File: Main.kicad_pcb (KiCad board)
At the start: 2 copper layers, 39 parts, among them J1 Conn_01x01_Female, J2 Conn_01x01_Female, J3 Conn_01x01_Female, J4 Conn_01x02_Female, J5 Conn_01x01_Female, Q1 CSD17307Q5A, Q2 CSD17307Q5A, Q3 Si6435ADQ, SW1 SW_Push, SW2 SW_Push, SW3 SW_Push, U1 LTC4002ES8-4.2, U2 BQ297xy, U3 LTC6995-1, U4 TPS2557

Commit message: finished traces
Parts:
- SW3: footprint Button_Switch_SMD:SW_SPST_B3U-1000P -> Button_Switch_SMD:SW_DIP_SPSTx01_Slide_6.7x4.1mm_W6.73mm_P2.54mm_LowProfile_JPin
- moved D2 188.3 mm to (217.4, 100.2), turned to 270 degrees
- moved TP1 180.4 mm to (217.4, 114.9)
- moved C3 177.9 mm to (210.0, 125.9)
- moved TP3 177.3 mm to (226.4, 103.6)
- moved D1 177.2 mm to (204.3, 98.7), turned to 180 degrees
- moved TP2 176.5 mm to (217.2, 125.9)
- moved C5 174.3 mm to (195.3, 73.3)
- moved J4 174.0 mm to (210.6, 73.0)
- moved R1 173.0 mm to (198.5, 98.7)
- moved SW1 171.7 mm to (210.1, 110.2), turned to 270 degrees
- moved C4 171.7 mm to (195.2, 77.3)
- moved J3 170.3 mm to (210.6, 53.0)
- moved J5 166.2 mm to (210.9, 97.9)
- moved J2 163.4 mm to (198.7, 51.3)
- moved C2 162.6 mm to (206.4, 81.3), turned to 90 degrees
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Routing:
- net GNDD: track 0.00 -> 103.7 mm, vias 0 -> 9
- net BAT: track 0.00 -> 94.9 mm
- net Net-(BT1-Pad2): track 0.00 -> 68.1 mm, vias 0 -> 2
- net Net-(C2-Pad1): track 0.00 -> 45.6 mm
- net Net-(C6-Pad1): track 0.00 -> 35.2 mm, vias 0 -> 2
- net Net-(D2-Pad1): track 0.00 -> 29.9 mm, vias 0 -> 2
- net Net-(J1-Pad1): track 0.00 -> 29.5 mm
- net Net-(J4-Pad1): track 0.00 -> 29.3 mm
- net Net-(Q2-Pad4): track 0.00 -> 23.7 mm, vias 0 -> 2
- net Net-(C3-Pad1): track 0.00 -> 23.3 mm
- net Net-(L1-Pad2): track 0.00 -> 22.2 mm
- net Net-(Q1-Pad4): track 0.00 -> 20.2 mm, vias 0 -> 2
- net Net-(Q1-Pad5): track 0.00 -> 17.5 mm
- net Net-(J2-Pad1): track 0.00 -> 17.5 mm
- net Net-(D1-Pad1): track 0.00 -> 12.6 mm, vias 0 -> 2
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- added copper zone on F.Cu, net +5V
- added copper zone on B.Cu, net GNDD
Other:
- board text added: "Cell Protection Circuit"
- board text added: "Short Switch"

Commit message: allot a work
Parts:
- moved TP1 172.0 mm to (53.3, 63.6)
- moved J5 159.6 mm to (55.0, 132.0)
- moved U3 154.3 mm to (62.0, 118.0)
- moved SW2 148.6 mm to (55.0, 119.0), turned to 270 degrees
- moved J3 147.1 mm to (75.0, 110.0)
- moved J4 147.1 mm to (75.0, 130.0)
- moved R3 142.0 mm to (53.0, 100.0), turned to 90 degrees
- moved R7 139.1 mm to (74.0, 91.0)
- moved Q1 136.9 mm to (65.5, 100.0), turned to 0 degrees
- moved J1 136.6 mm to (54.0, 107.0)
- moved J2 136.6 mm to (74.0, 107.0)
- moved C3 134.8 mm to (79.0, 94.0), turned to 270 degrees
- moved R4 133.5 mm to (57.0, 100.0), turned to 90 degrees
- moved TP3 132.4 mm to (96.0, 126.4)
- moved SW3 132.4 mm to (56.0, 84.0)
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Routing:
- net BAT: track 94.9 -> 52.9 mm
- net Net-(BT1-Pad2): track 68.1 -> 102.5 mm
- net Net-(J2-Pad1): track 17.5 -> 39.5 mm, vias 0 -> 2
- net GNDD: track 103.7 -> 82.5 mm, vias 9 -> 8
- net Net-(C2-Pad1): track 45.6 -> 29.8 mm, vias 0 -> 2
- net Net-(C6-Pad1): track 35.2 -> 50.8 mm, vias 2 -> 0
- net Net-(C3-Pad1): track 23.3 -> 8.76 mm
- net Net-(J1-Pad1): track 29.5 -> 15.2 mm
- net Net-(L1-Pad2): track 22.2 -> 8.34 mm
- net Net-(R3-Pad2): track 6.94 -> 20.7 mm
- net Net-(D2-Pad1): track 29.9 -> 18.8 mm, vias 2 -> 0
- net Net-(J4-Pad1): track 29.3 -> 18.3 mm
- net Net-(Q3-Pad3): track 0.00 -> 10.6 mm
- net Net-(Q2-Pad4): track 23.7 -> 14.9 mm, vias 2 -> 0
- net Net-(R11-Pad1): track 8.33 -> 3.74 mm
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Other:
- board text added: "Bat+"
- board text added: "Bat-"
- board text added: "Battery Protection"
- board text added: "Charging Circuit"
- board text added: "Ground"
- board text added: "Load Switch"
- board text added: "Timer Circuit"
- board text removed: "Cell Protection Circuit"
- board text removed: "Short Switch"

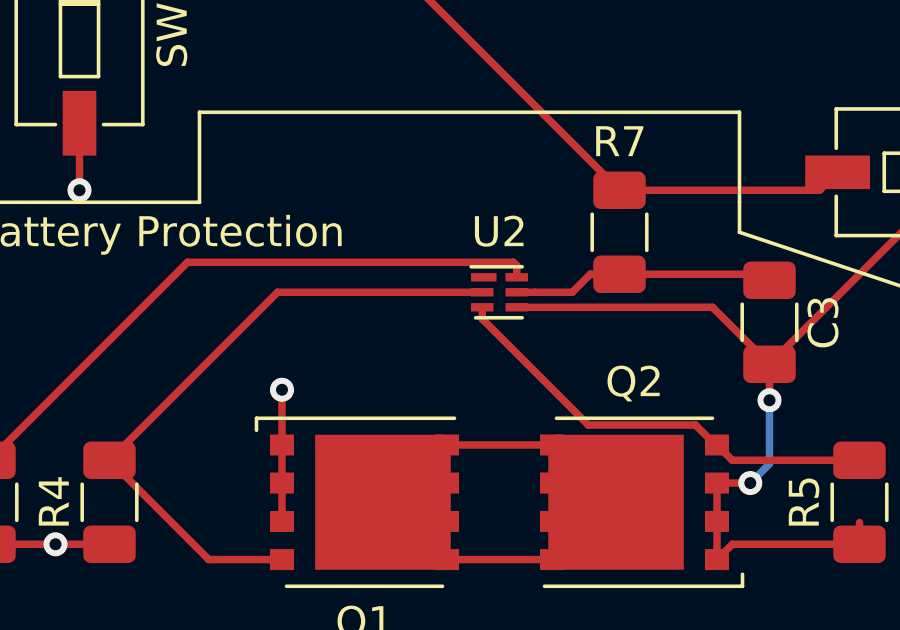
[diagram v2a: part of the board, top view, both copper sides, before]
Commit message: still need breakout board for bq29707
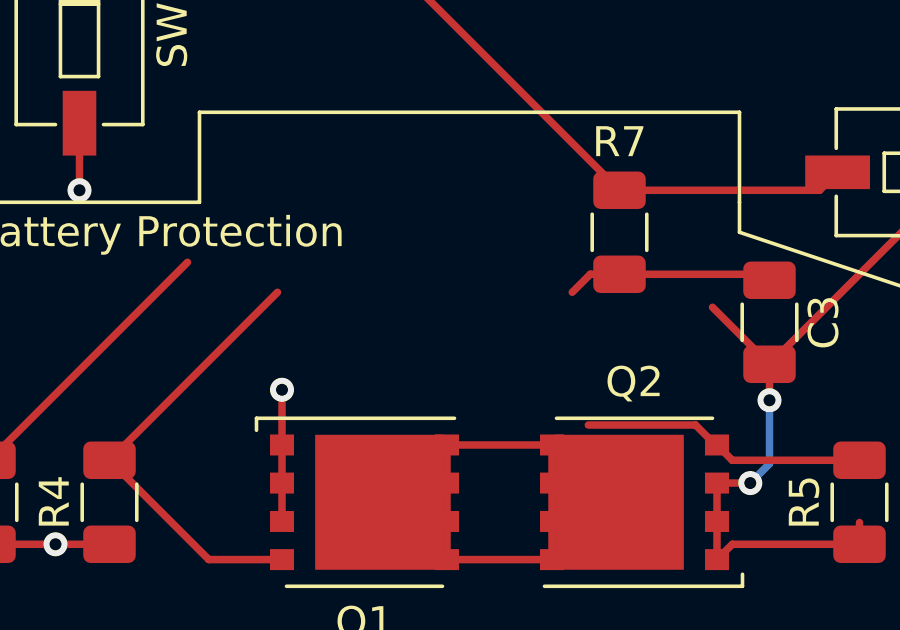
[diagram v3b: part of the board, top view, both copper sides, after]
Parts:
- removed U2: BQ297xy, Package_SON:WSON-6_1.5x1.5mm_P0.5mm
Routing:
- net Net-(R3-Pad2): track 20.7 -> 9.33 mm
- net Net-(Q1-Pad4): track 21.9 -> 15.0 mm
- net Net-(BT1-Pad2): track 102.5 -> 96.0 mm
- net Net-(Q2-Pad4): track 14.9 -> 9.53 mm
- net Net-(C3-Pad1): track 8.76 -> 6.91 mm
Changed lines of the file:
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@@
     (thickness 1.6)
     (drawings 30)
-    (tracks 205)
+    (tracks 196)
     (zones 0)
-    (modules 39)
-    (nets 29)
+    (modules 38)
+    (nets 28)
   )
   (page A4)
@@
     (solder_mask_min_width 0.25)
     (aux_axis_origin 0 0)
-    (visible_elements FFFDFF7F)
+    (visible_elements 7FFFFFFF)
     (pcbplotparams
       (layerselection 0x010fc_ffffffff)
@@
   (net 23 "Net-(R3-Pad2)")
   (net 24 "Net-(R11-Pad1)")
-  (net 25 "Net-(U2-Pad1)")
-  (net 26 "Net-(U4-Pad3)")
-  (net 27 "Net-(U4-Pad8)")
-  (net 28 "Net-(U4-Pad6)")
+  (net 25 "Net-(U4-Pad3)")
+  (net 26 "Net-(U4-Pad8)")
+  (net 27 "Net-(U4-Pad6)")
   (net_class Default "This is the default net class."
     (clearance 0.2)
@@
     (add_net "Net-(R11-Pad1)")
     (add_net "Net-(R3-Pad2)")
-    (add_net "Net-(U2-Pad1)")
     (add_net "Net-(U4-Pad3)")
     (add_net "Net-(U4-Pad6)")
@@
     )
   )
-  (module Package_SON:WSON-6_1.5x1.5mm_P0.5mm (layer F.Cu)
-    (at 70 93)
-    (descr "WSON6, http://www.ti.com/lit/ds/symlink/tlv702.pdf")
-    (tags WSON6_1.5x1.5mm_P0.5mm)
-    (attr smd)
-    (fp_text reference U2 (at 0 -2) (layer F.SilkS)
-      (effects (font (size 1 1) (thickness 0.15)))
-    )
-    (fp_text value BQ297xy (at 0 2) (layer F.Fab)
-      (effects (font (size 1 1) (thickness 0.15)))
-    )
-    (fp_text user %R (at 0.005 0) (layer F.Fab)
-      (effects (font (size 0.4 0.4) (thickness 0.05)))
-    )
-    (fp_line (start -0.945 -0.85) (end 0.755 -0.85) (layer F.SilkS) (width 0.12))
-    (fp_line (start -0.795 0.85) (end 0.755 0.85) (layer F.SilkS) (width 0.12))
-    (fp_line (start -0.495 -0.78) (end -0.775 -0.5) (layer F.Fab) (width 0.1))
-    (fp_line (start 0.785 -0.78) (end -0.495 -0.78) (layer F.Fab) (width 0.1))
-    (fp_line (start -0.775 -0.5) (end -0.775 0.78) (layer F.Fab) (width 0.1))
-    (fp_line (start -0.775 0.78) (end 0.785 0.78) (layer F.Fab) (width 0.1))
-    (fp_line (start 0.785 -0.78) (end 0.785 0.78) (layer F.Fab) (width 0.1))
-    (fp_line (start 1.2 -1.02) (end 1.2 1.02) (layer F.CrtYd) (width 0.05))
-    (fp_line (start 1.2 -1.02) (end -1.2 -1.02) (layer F.CrtYd) (width 0.05))
-    (fp_line (start -1.2 1.02) (end 1.2 1.02) (layer F.CrtYd) (width 0.05))
-    (fp_line (start -1.2 1.02) (end -1.2 -1.02) (layer F.CrtYd) (width 0.05))
-    (pad 1 smd rect (at -0.525 -0.5 270) (size 0.28 0.85) (layers F.Cu F.Paste F.Mask)
-      (net 25 "Net-(U2-Pad1)"))
-    (pad 2 smd rect (at -0.575 0 270) (size 0.28 0.75) (layers F.Cu F.Paste F.Mask)
-      (net 20 "Net-(Q1-Pad4)"))
-    (pad 3 smd rect (at -0.575 0.5 270) (size 0.28 0.75) (layers F.Cu F.Paste F.Mask)
-      (net 21 "Net-(Q2-Pad4)"))
-    (pad 4 smd rect (at 0.575 0.5 270) (size 0.28 0.75) (layers F.Cu F.Paste F.Mask)
-      (net 2 "Net-(BT1-Pad2)"))
-    (pad 5 smd rect (at 0.575 0 270) (size 0.28 0.75) (layers F.Cu F.Paste F.Mask)
-      (net 7 "Net-(C3-Pad1)"))
-    (pad 6 smd rect (at 0.575 -0.5 270) (size 0.28 0.75) (layers F.Cu F.Paste F.Mask)
-      (net 23 "Net-(R3-Pad2)"))
-    (model ${KISYS3DMOD}/Package_SON.3dshapes/WSON-6_1.5x1.5mm_P0.5mm.wrl
-      (at (xyz 0 0 0))
-      (scale (xyz 1 1 1))
-      (rotate (xyz 0 0 0))
-    )
-  )
   (module Package_TO_SOT_SMD:TSOT-23-6 (layer F.Cu)
     (at 62 118)
@@
       (net 9 "Net-(C6-Pad1)"))
     (pad 3 smd rect (at 0 1.3) (size 0.5 0.35) (layers F.Cu F.Paste F.Mask)
-      (net 26 "Net-(U4-Pad3)"))
+      (net 25 "Net-(U4-Pad3)"))
     (pad 4 smd rect (at 0 1.95) (size 0.5 0.35) (layers F.Cu F.Paste F.Mask)
       (net 16 "Net-(J2-Pad1)"))
@@
       (net 24 "Net-(R11-Pad1)"))
     (pad 8 smd rect (at 2.8 0) (size 0.5 0.35) (layers F.Cu F.Paste F.Mask)
-      (net 27 "Net-(U4-Pad8)"))
+      (net 26 "Net-(U4-Pad8)"))
     (pad 6 smd rect (at 2.8 1.3) (size 0.5 0.35) (layers F.Cu F.Paste F.Mask)
-      (net 28 "Net-(U4-Pad6)"))
+      (net 27 "Net-(U4-Pad6)"))
     (pad 1 smd rect (at 1.4 0.975) (size 1.65 2.4) (layers F.Cu F.Paste F.Mask)
       (net 5 GNDD))
@@
   (segment (start 77.25 101.91) (end 77.25 100.64) (width 0.25) (layer F.Cu) (net 2))
   (segment (start 77.1 93.5) (end 79 95.4) (width 0.25) (layer F.Cu) (net 2))
-  (segment (start 70.575 93.5) (end 77.1 93.5) (width 0.25) (layer F.Cu) (net 2))
   (segment (start 77.25 99.36) (end 78.36 99.36) (width 0.25) (layer F.Cu) (net 2))
   (segment (start 78.36 99.36) (end 78.36 99.36) (width 0.25) (layer F.Cu) (net 2))
@@
   (segment (start 102.675 93.635) (end 102.599999 93.559999) (width 0.25) (layer F.Cu) (net 6))
   (segment (start 103.7 93.635) (end 102.675 93.635) (width 0.25) (layer F.Cu) (net 6))
-  (segment (start 71.2 93) (end 70.575 93) (width 0.25) (layer F.Cu) (net 7))
-  (segment (start 72.425 93) (end 71.2 93) (width 0.25) (layer F.Cu) (net 7))
   (segment (start 73.025 92.4) (end 72.425 93) (width 0.25) (layer F.Cu) (net 7))
   (segment (start 74 92.4) (end 73.025 92.4) (width 0.25) (layer F.Cu) (net 7))
@@
   (segment (start 60.31 101.91) (end 62.75 101.91) (width 0.25) (layer F.Cu) (net 20))
   (segment (start 57 98.6) (end 60.31 101.91) (width 0.25) (layer F.Cu) (net 20))
-  (segment (start 62.6 93) (end 69.425 93) (width 0.25) (layer F.Cu) (net 20))
   (segment (start 57 98.6) (end 62.6 93) (width 0.25) (layer F.Cu) (net 20))
   (segment (start 77.2 98.09) (end 77.25 98.09) (width 0.25) (layer F.Cu) (net 21))
   (segment (start 76.534999 97.424999) (end 77.2 98.09) (width 0.25) (layer F.Cu) (net 21))
   (segment (start 72.959999 97.424999) (end 76.534999 97.424999) (width 0.25) (layer F.Cu) (net 21))
-  (segment (start 69.425 93.89) (end 72.959999 97.424999) (width 0.25) (layer F.Cu) (net 21))
-  (segment (start 69.425 93.5) (end 69.425 93.89) (width 0.25) (layer F.Cu) (net 21))
   (segment (start 77.76 98.6) (end 77.25 98.09) (width 0.25) (layer F.Cu) (net 21))
   (segment (start 82 98.6) (end 77.76 98.6) (width 0.25) (layer F.Cu) (net 21))
@@
   (segment (start 99.6 96.939998) (end 96.999999 99.539999) (width 0.25) (layer F.Cu) (net 22))
   (segment (start 99.6 94.46) (end 99.6 96.939998) (width 0.25) (layer F.Cu) (net 22))
-  (segment (start 70.575 92.11) (end 70.575 92.5) (width 0.25) (layer F.Cu) (net 23))
-  (segment (start 70.465 92) (end 70.575 92.11) (width 0.25) (layer F.Cu) (net 23))
-  (segment (start 59.6 92) (end 70.465 92) (width 0.25) (layer F.Cu) (net 23))
   (segment (start 53 98.6) (end 59.6 92) (width 0.25) (layer F.Cu) (net 23))
   (segment (start 96.4 117.4) (end 96.4 116.975) (width 0.25) (layer F.Cu) (net 24))

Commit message: Finished, should be reviewed
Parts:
- added J6: Conn_01x03, Connector_PinSocket_2.54mm:PinSocket_1x03_P2.54mm_Vertical, F.Cu at (68.7, 92.7)
- added J7: Conn_01x03, Connector_PinSocket_2.54mm:PinSocket_1x03_P2.54mm_Vertical, F.Cu at (83.9, 92.7)
- added TP4: TestPoint, Connector_PinHeader_2.00mm:PinHeader_1x01_P2.00mm_Vertical, F.Cu at (113.8, 121.0)
- moved C1 13.6 mm to (108.0, 96.6)
- moved C4 13.6 mm to (116.1, 91.6)
- moved C5 13.6 mm to (112.0, 91.6)
- moved D1 13.6 mm to (128.0, 99.0)
- moved D2 13.6 mm to (129.0, 106.0)
- moved L1 13.6 mm to (122.0, 102.0)
- moved Q3 13.6 mm to (114.0, 105.0)
- moved R1 13.6 mm to (133.0, 97.6)
- moved R2 13.6 mm to (108.0, 102.0)
- moved R6 13.6 mm to (122.0, 97.0)
- moved U1 13.6 mm to (114.0, 97.0)
- moved C2 13.5 mm to (120.9, 93.1)
- moved SW1 13.5 mm to (97.9, 91.4)
- moved R3 10.5 mm to (60.2, 107.6)
- moved Q1 8.03 mm to (68.1, 107.6)
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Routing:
- net Net-(J7-Pad3): track 9.33 -> 27.2 mm
- net Net-(J6-Pad2): track 15.0 -> 27.0 mm
- net Net-(J6-Pad3): track 9.53 -> 20.1 mm, vias 0 -> 2
- net Net-(C7-Pad1): track 10.0 -> 20.2 mm
- net Net-(BT1-Pad2): track 96.0 -> 105.2 mm
- net BAT: track 52.9 -> 61.8 mm
- net Net-(C3-Pad1): track 6.91 -> 11.4 mm
- net +5V: track 0.00 -> 1.25 mm
- net Net-(C2-Pad1): track 29.8 -> 30.5 mm, vias 2 -> 1
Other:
- board text added: "Battery Protection Circuit"
- board text added: "Pout"
- board text added: "Short Switch"
- board text removed: "Battery Protection"

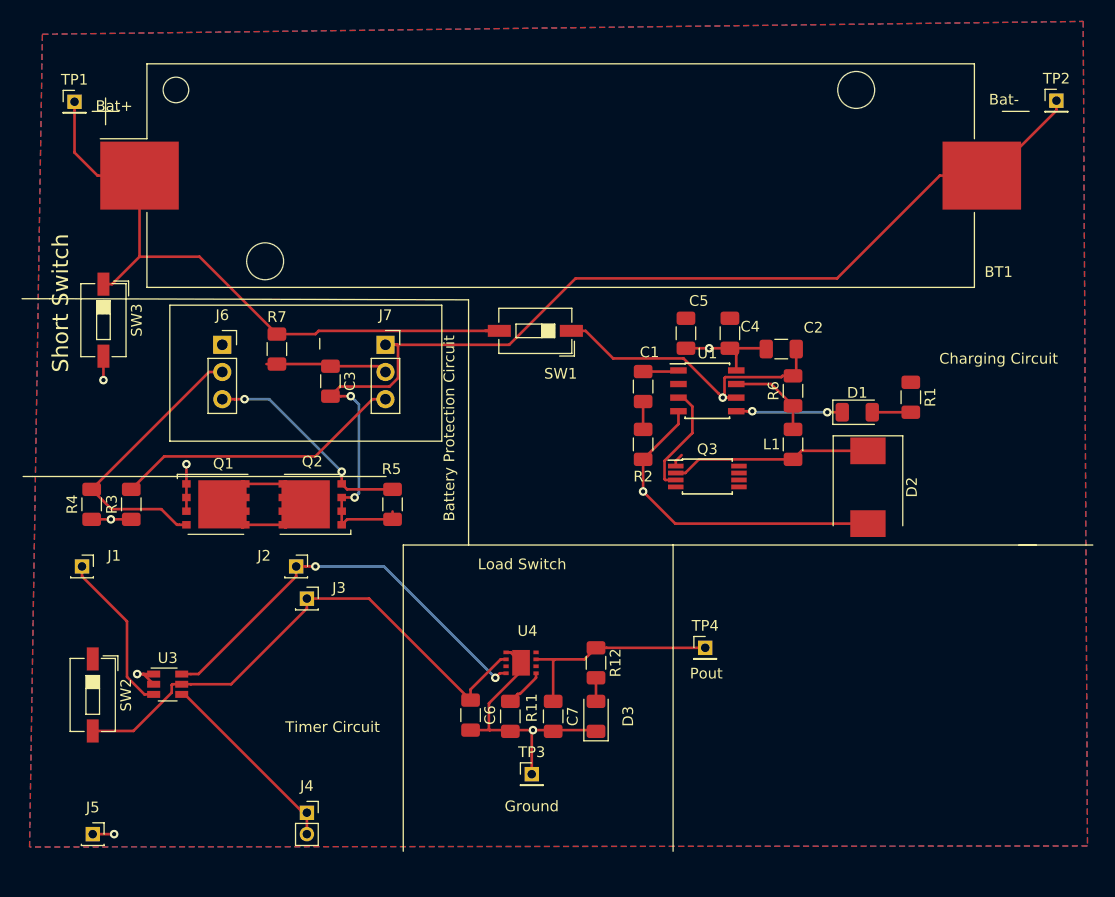
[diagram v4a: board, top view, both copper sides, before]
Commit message: added edge cut layer
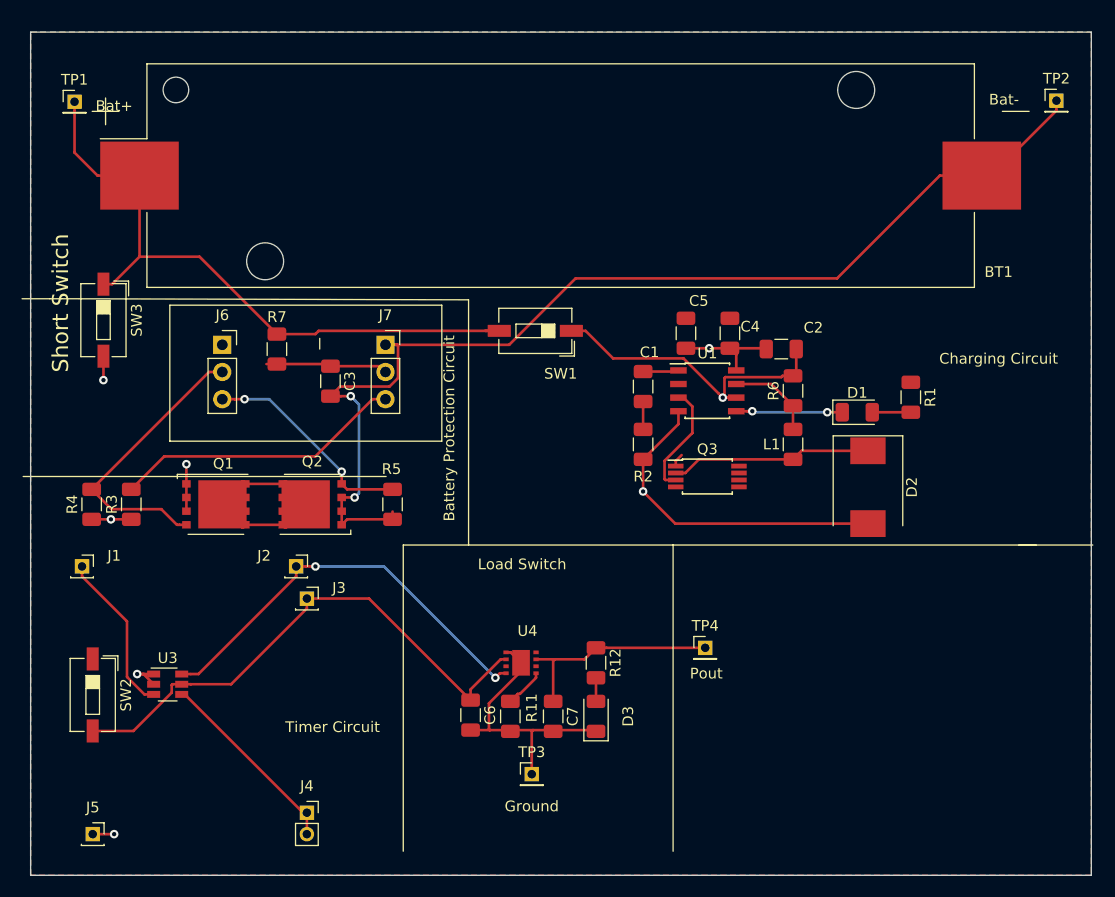
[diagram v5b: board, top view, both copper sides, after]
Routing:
- net GNDD: vias 8 -> 7
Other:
- board outline added: 99.1 x 78.7 mm
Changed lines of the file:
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@@
     (thickness 1.6)
     (drawings 29)
-    (tracks 227)
+    (tracks 226)
     (zones 0)
     (modules 41)
@@
     )
   )
+  (gr_line (start 50.8 142.24) (end 50.8 63.5) (layer Edge.Cuts) (width 0.05))
+  (gr_line (start 149.86 142.24) (end 50.8 142.24) (layer Edge.Cuts) (width 0.05))
+  (gr_line (start 149.86 63.5) (end 149.86 142.24) (layer Edge.Cuts) (width 0.05))
+  (gr_line (start 50.8 63.5) (end 149.86 63.5) (layer Edge.Cuts) (width 0.05))
   (gr_text "Short Switch" (at 53.6 88.8 90) (layer F.SilkS)
     (effects (font (size 1.5 1.5) (thickness 0.3)))
@@
   (gr_line (start 77.8 92.1) (end 77.8 93.1) (layer F.SilkS) (width 0.12))
   (gr_line (start 85.6 111.4) (end 85.6 140) (layer F.SilkS) (width 0.12))
-  (gr_line (start 150 140) (end 50 140) (layer Eco1.User) (width 0.15))
-  (gr_line (start 150 60) (end 150 140) (layer Eco1.User) (width 0.15))
-  (gr_line (start 50 140) (end 50 60) (layer Eco1.User) (width 0.15))
-  (gr_line (start 50 60) (end 150 60) (layer Eco1.User) (width 0.15))
   (segment (start 54.9 70.925) (end 54.9 70) (width 0.25) (layer F.Cu) (net 1))
   (segment (start 54.9 74.75) (end 54.9 70.925) (width 0.25) (layer F.Cu) (net 1))
@@
   (segment (start 103.485001 128.685001) (end 103.6 128.8) (width 0.25) (layer F.Cu) (net 5))
   (segment (start 97.714999 128.685001) (end 103.485001 128.685001) (width 0.25) (layer F.Cu) (net 5))
-  (via (at 97.714999 128.685001) (size 0.8) (drill 0.4) (layers F.Cu B.Cu) (net 5))
-  (segment (start 97.6 128.8) (end 97.714999 128.685001) (width 0.25) (layer F.Cu) (net 5))
-  (segment (start 97.6 132.8) (end 97.6 128.8) (width 0.25) (layer F.Cu) (net 5))
   (segment (start 95.625 121.425) (end 96.6 122.4) (width 0.25) (layer F.Cu) (net 5))
   (segment (start 95.2 121.425) (end 95.625 121.425) (width 0.25) (layer F.Cu) (net 5))
@@
   (segment (start 58.3 109) (end 60.2 109) (width 0.25) (layer F.Cu) (net 5))
   (via (at 58.3 109) (size 0.8) (drill 0.4) (layers F.Cu B.Cu) (net 5))
+  (segment (start 97.6 128.8) (end 97.714999 128.685001) (width 0.25) (layer F.Cu) (net 5))
+  (segment (start 97.6 132.8) (end 97.6 128.8) (width 0.25) (layer F.Cu) (net 5))
   (segment (start 116.7 97.635) (end 115.435 97.635) (width 0.25) (layer F.Cu) (net 6))
   (segment (start 115.435 97.635) (end 115.435 97.635) (width 0.25) (layer F.Cu) (net 6))
@@
   (segment (start 94.625 123.375) (end 94.2 123.8) (width 0.25) (layer F.Cu) (net 16))
   (segment (start 94.2 123.8) (end 94.2 123.8) (width 0.25) (layer F.Cu) (net 16))
-  (via (at 94.2 123.8) (size 0.8) (drill 0.4) (layers F.Cu B.Cu) (net 16))
+  (via (at 94.2 123.8) (size 0.8) (drill 0.4) (layers F.Cu B.Cu) (net 16) (status 1000000))
   (segment (start 83.8 113.4) (end 94.2 123.8) (width 0.25) (layer B.Cu) (net 16))
   (segment (start 77.4 113.4) (end 83.8 113.4) (width 0.25) (layer B.Cu) (net 16))
@@
     (polygon
       (pts
-        (xy 149.5 139.5) (xy 50.7 139.6) (xy 51.9 63.7) (xy 149.1 62.5)
+        (xy 50.8 63.5) (xy 149.86 63.5) (xy 149.86 142.24) (xy 50.8 142.24)
       )
     )
@@
     (polygon
       (pts
-        (xy 149.5 139.5) (xy 50.7 139.6) (xy 51.9 63.7) (xy 149.1 62.5)
+        (xy 50.8 63.5) (xy 149.86 63.5) (xy 149.86 142.24) (xy 50.8 142.24)
       )
     )

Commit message: reviewed footprints
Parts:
- U3: footprint Package_TO_SOT_SMD:TSOT-23-6 -> Package_TO_SOT_SMD:TSOT-23-6_HandSoldering
- moved U3 2.44 mm to (66.0, 124.5)
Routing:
- net GNDD: track 82.2 -> 86.3 mm
- net Net-(C6-Pad1): track 50.8 -> 54.6 mm
- net Net-(J1-Pad1): track 15.2 -> 17.3 mm
- net Net-(J2-Pad1): track 39.5 -> 38.0 mm
- net Net-(J4-Pad1): track 18.3 -> 17.6 mm
